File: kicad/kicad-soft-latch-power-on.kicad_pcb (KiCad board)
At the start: 2 copper layers, 21.1 x 9.6 mm, 8 parts, among them J1 Conn_01x03, J2 Conn_01x03, Q1 SI9942DY

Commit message: added render
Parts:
- J1, J2: moved to B.Cu
- turned J1 to 0 degrees
- turned J2 to 0 degrees

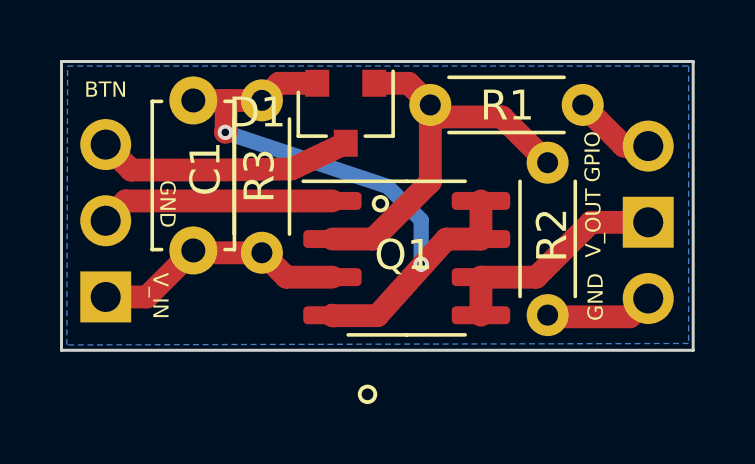
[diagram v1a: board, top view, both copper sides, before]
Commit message: add reverse polarity protection
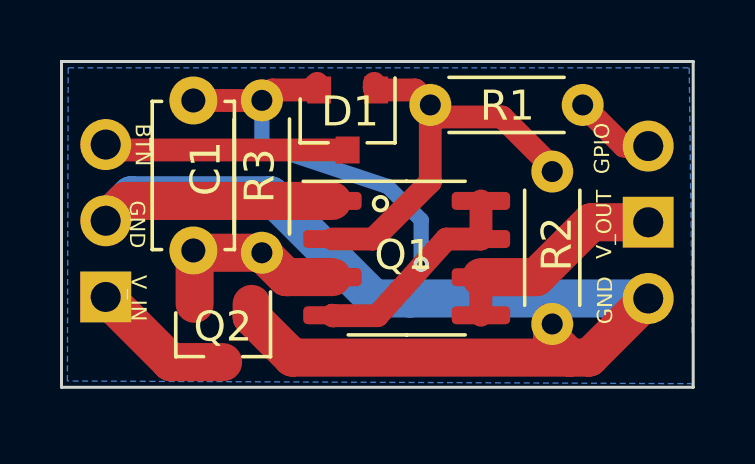
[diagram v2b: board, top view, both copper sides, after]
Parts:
- added Q2: AO3401A, Package_TO_SOT_SMD:SOT-23, F.Cu at (128.1, 112.9)
- moved R2 0.33 mm to (139.0, 107.5)
- moved D1 0.23 mm to (132.2, 105.8)
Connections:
- C1 pad 1: V_IN -> Net-(C1-Pad1)
- Q1 pad 3: V_IN -> Net-(C1-Pad1)
- R3 pad 1: V_IN -> Net-(C1-Pad1)
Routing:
- net GND: track 11.5 -> 45.1 mm
- net Net-(C1-Pad1): track 0.00 -> 6.80 mm
- net V_IN: track 8.57 -> 4.82 mm
- net Net-(C1-Pad2): track 21.6 -> 20.7 mm, vias 2 -> 1
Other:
- board size 21.1 x 9.6 mm -> 21.1 x 10.9 mm

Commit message: final version with TH parts
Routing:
- net GND: track 45.1 -> 23.4 mm, vias 0 -> 2
